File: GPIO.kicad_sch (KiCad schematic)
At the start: 8 parts, among them J12 gnd, J13 ADC, J14 Conn_01x08_Male, J15 ADC, J16 Conn_01x08_Male, J17 Conn_01x08_Male

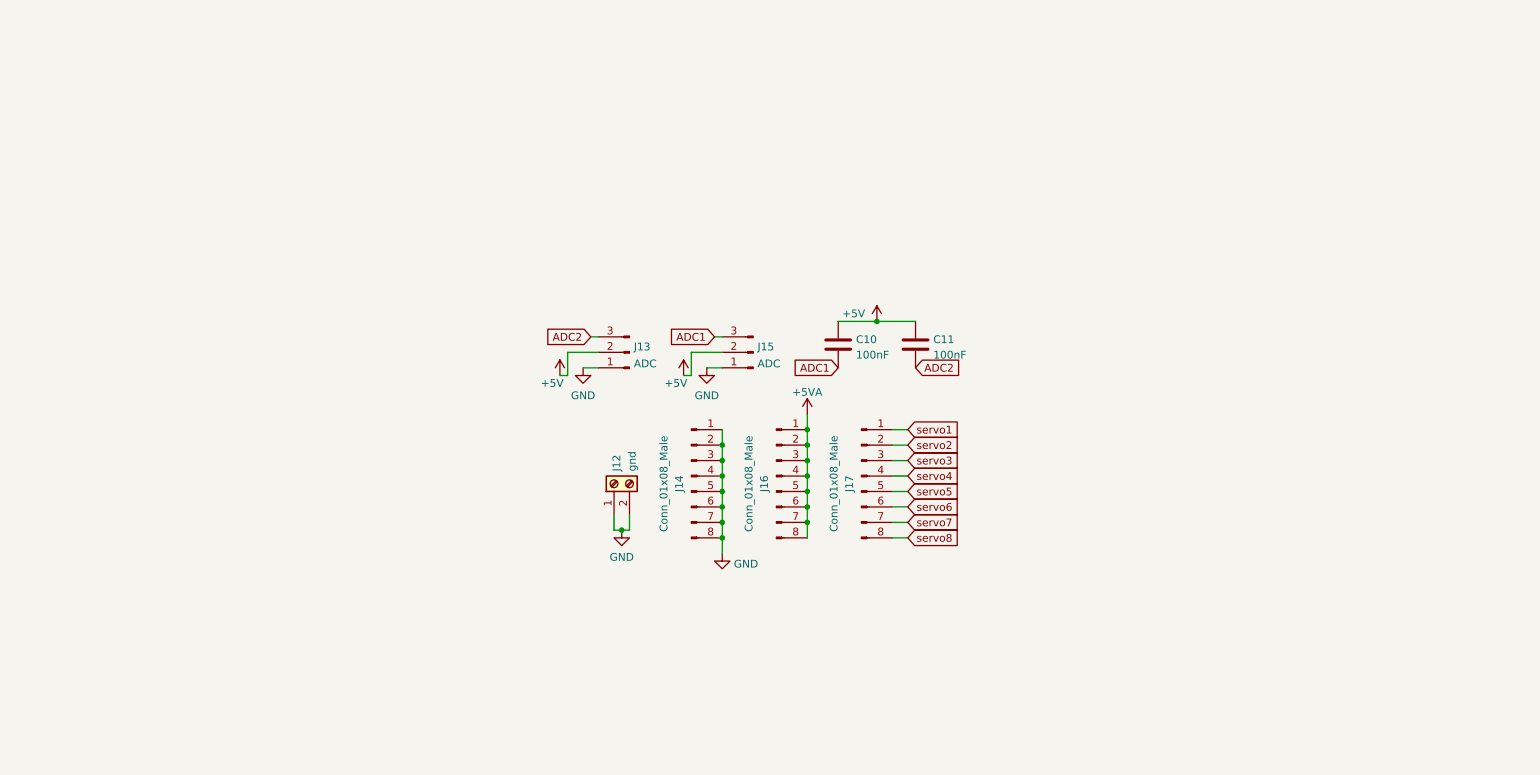
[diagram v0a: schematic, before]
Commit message: changed PCB layout. I want to change more
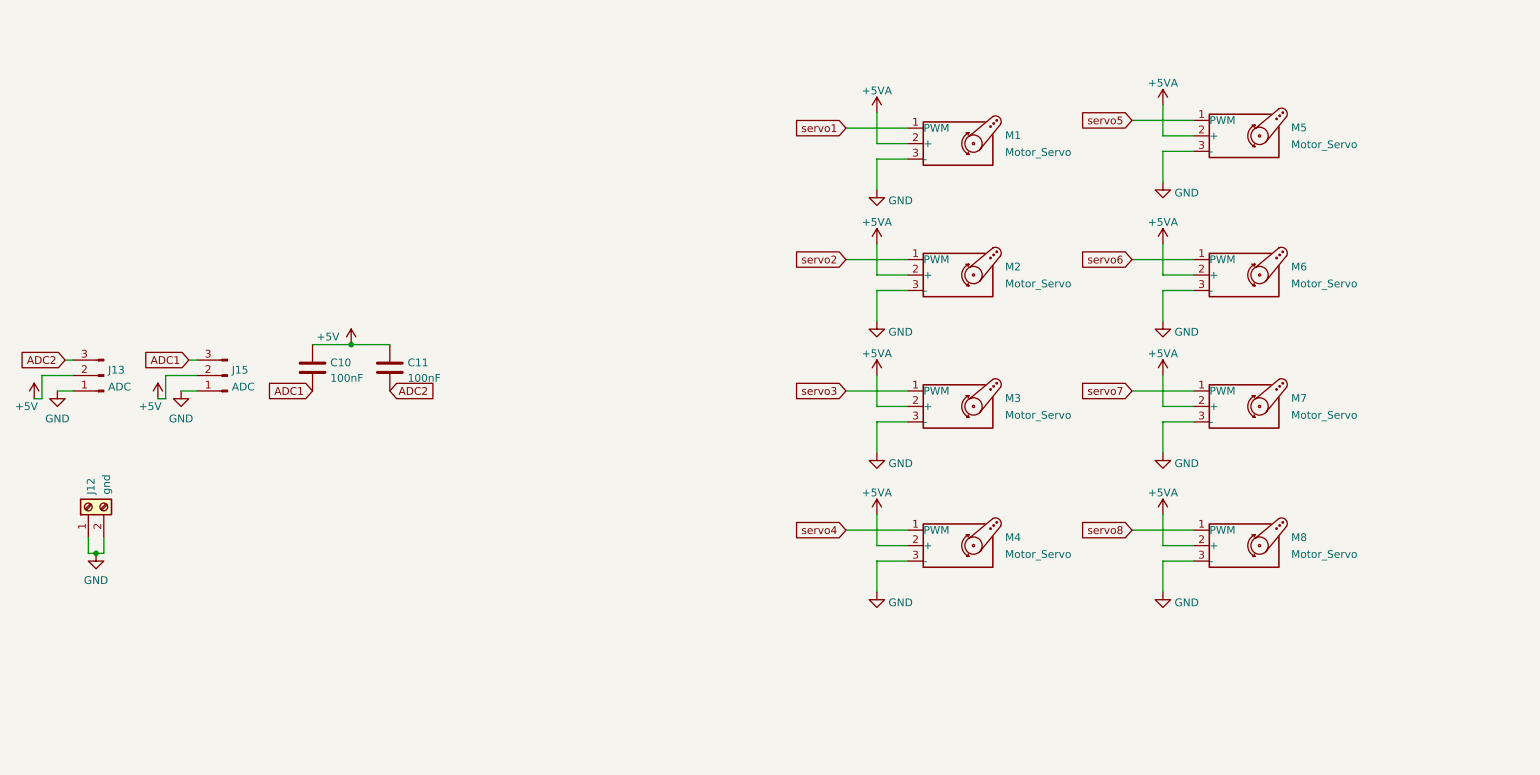
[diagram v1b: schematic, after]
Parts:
- removed J14, J16, J17: Conn_01x08_Male, Connector_PinHeader_2.54mm:PinHeader_1x08_P2.54mm_Vertical, symbol Connector:Conn_01x08_Male
- added M1, M2, M3, M4, M5, M6, M7, M8: Motor_Servo, Connector_PinHeader_2.54mm:PinHeader_1x03_P2.54mm_Vertical, symbol Motor:Motor_Servo
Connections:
- net +5VA: now also M1.2 (+), M2.2 (+), M3.2 (+), M4.2 (+), M5.2 (+), M6.2 (+), M7.2 (+), M8.2 (+)
- net GND: now also M1.3 (-), M2.3 (-), M3.3 (-), M4.3 (-), M5.3 (-), M6.3 (-), M7.3 (-), M8.3 (-)
- net servo1: now also M1.1 (PWM)
- net servo2: now also M2.1 (PWM)
- net servo3: now also M3.1 (PWM)
- net servo4: now also M4.1 (PWM)
- net servo5: now also M5.1 (PWM)
- net servo6: now also M6.1 (PWM)
- net servo7: now also M7.1 (PWM)
- net servo8: now also M8.1 (PWM)
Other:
- moved on the sheet: C10, C11, J12, J13, J15

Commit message: redone the switch connectors to accomodate a current sense print. Rearranged parts and updated silk texts to be 50% of their original size
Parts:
- removed J12: gnd, TerminalBlock_Phoenix:TerminalBlock_Phoenix_MKDS-1,5-2-5.08_1x02_P5.08mm_Horizontal, symbol Connector:Screw_Terminal_01x02
- renumbered C10 to C801, C11 to C802, J13 to J801, J15 to J802, M1 to M801, M2 to M802, M3 to M803, M4 to M804, M5 to M805, M6 to M806, M7 to M807, M8 to M808

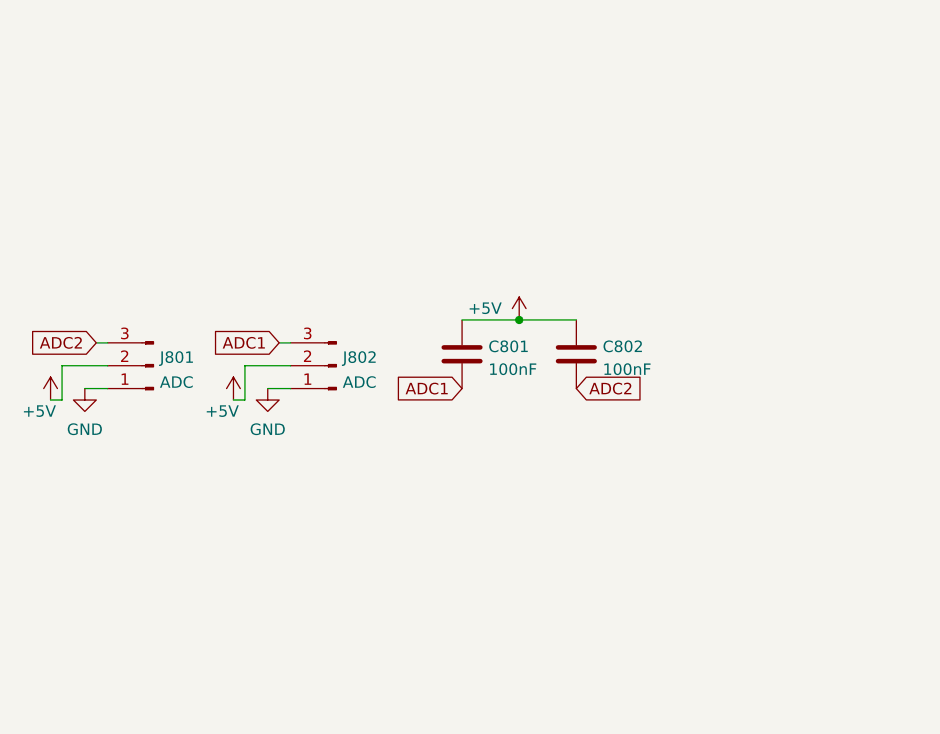
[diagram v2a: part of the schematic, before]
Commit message: added something to debug the channel buttons
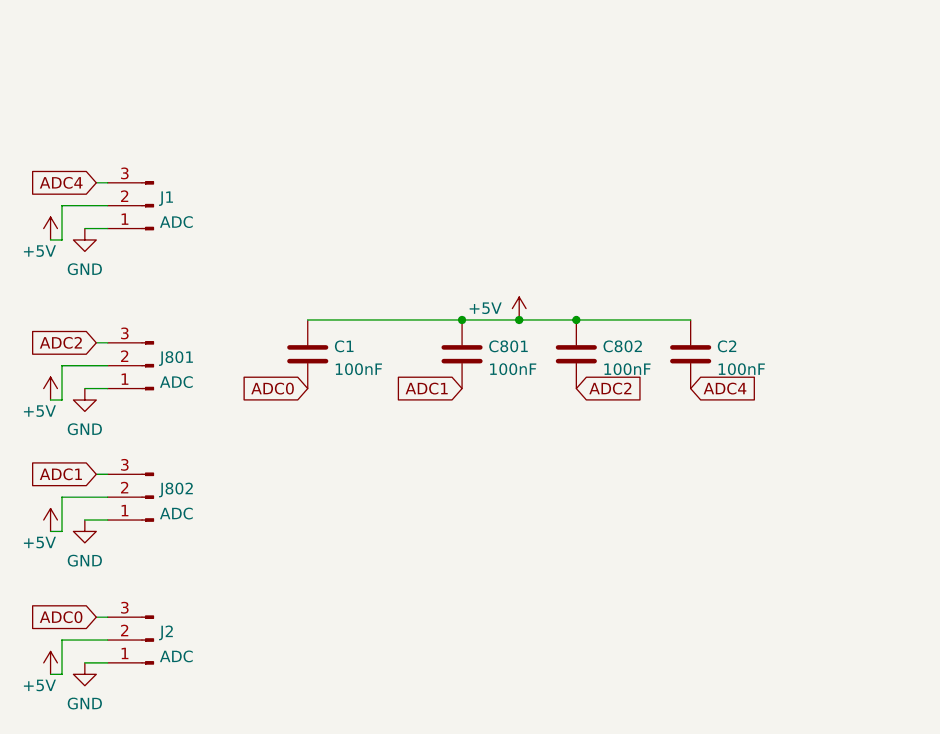
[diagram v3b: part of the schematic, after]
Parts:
- added C1, C2: 100nF, Capacitor_SMD:C_0805_2012Metric, symbol Device:C
- added J1, J2: ADC, Connector_PinHeader_2.54mm:PinHeader_1x03_P2.54mm_Vertical, symbol Connector:Conn_01x03_Male
- C801, C802: footprint Capacitor_THT:C_Disc_D3.0mm_W1.6mm_P2.50mm -> Capacitor_SMD:C_0805_2012Metric
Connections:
- net +5V: now also C1.1, C2.1, J1.2 (Pin_2), J2.2 (Pin_2)
- net GND: now also J1.1 (Pin_1), J2.1 (Pin_1)
- new net ADC0: C1.2, J2.3 (Pin_3)
- new net ADC4: C2.2, J1.3 (Pin_3)
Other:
- moved on the sheet: J802

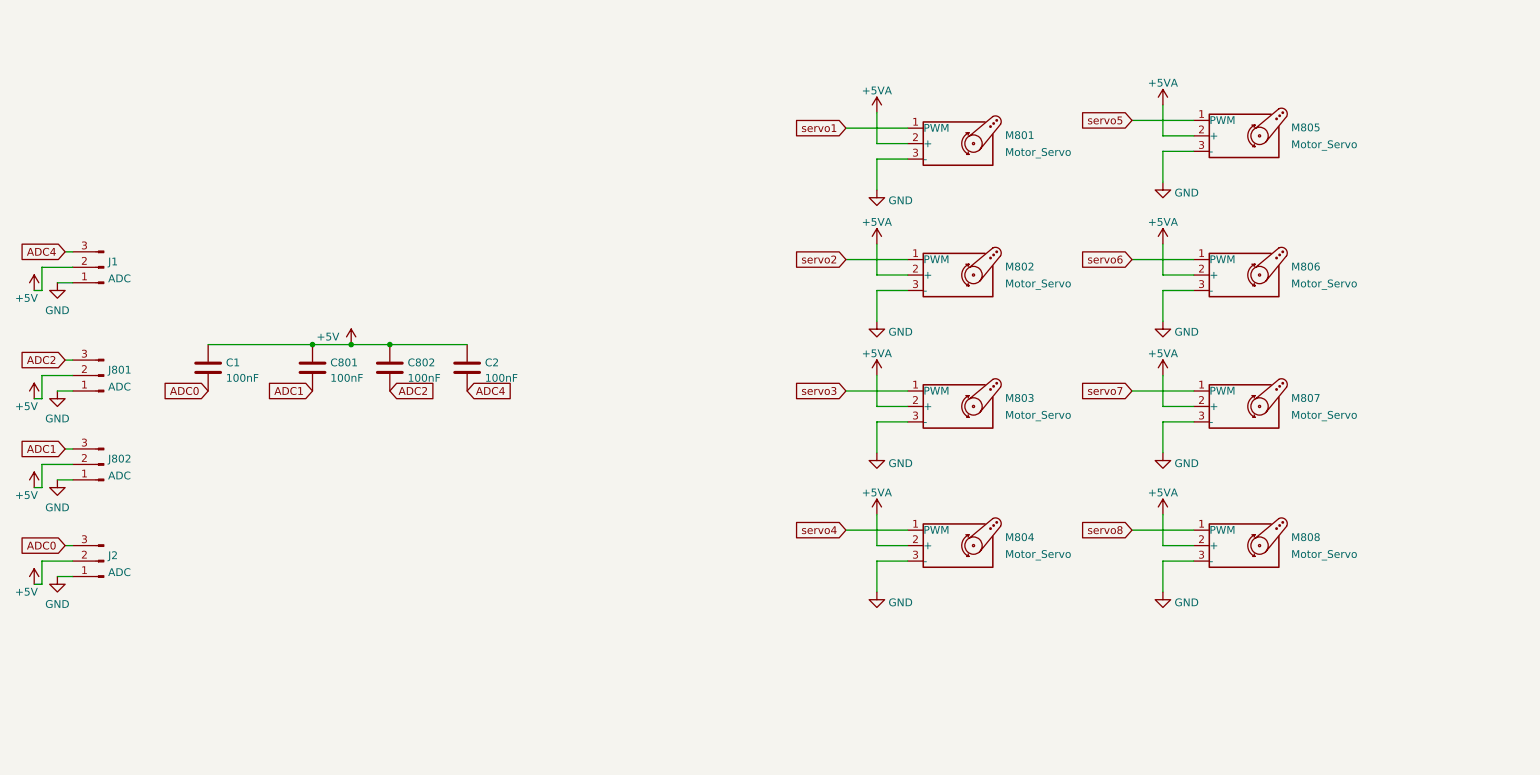
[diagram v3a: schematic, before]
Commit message: redid this project. I want to use an atmega328 so I ditched some IO. I retained 4 servo, 1 H-bridge (should make it double), 3 relays, 6 GPIO, 1 potentiometer and loconet interface. And I still have a config button
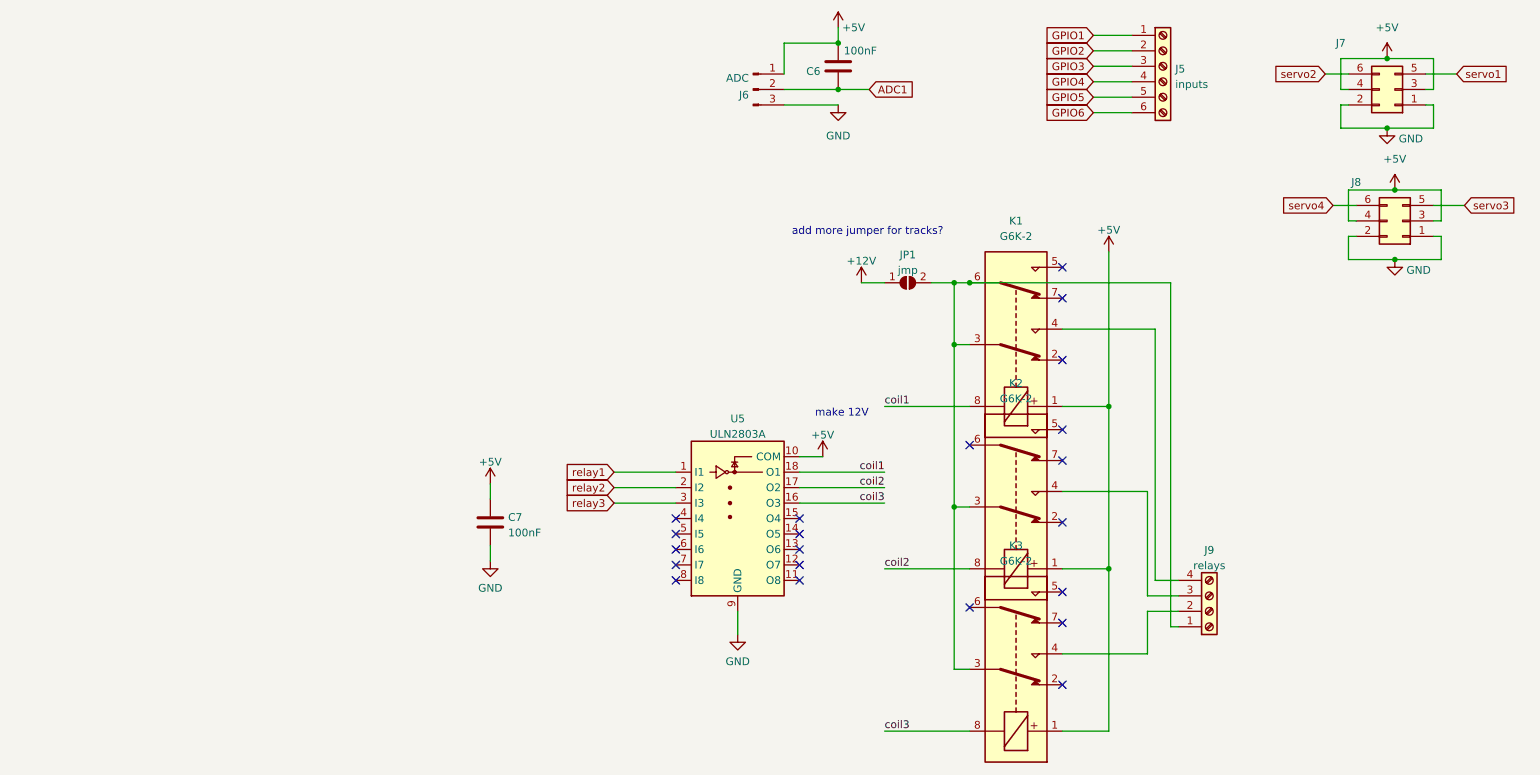
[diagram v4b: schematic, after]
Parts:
- removed C1, C2, C801, C802: 100nF, Capacitor_SMD:C_0805_2012Metric, symbol Device:C
- removed J1, J2, J801: ADC, Connector_PinHeader_2.54mm:PinHeader_1x03_P2.54mm_Vertical, symbol Connector:Conn_01x03_Male
- removed M801, M802, M803, M804, M805, M806, M807, M808: Motor_Servo, Connector_PinHeader_2.54mm:PinHeader_1x03_P2.54mm_Vertical, symbol Motor:Motor_Servo
- added C6, C7: 100nF, Capacitor_SMD:C_0805_2012Metric, symbol Device:C
- added J5: inputs, TerminalBlock_Phoenix:TerminalBlock_Phoenix_MPT-0,5-8-2.54_1x06_P2.54mm_Horizontal, symbol Connector:Screw_Terminal_01x06
- added J7, J8: Conn_02x03_Odd_Even, Connector_PinHeader_2.54mm:PinHeader_2x03_P2.54mm_Vertical_SMD, symbol Connector_Generic:Conn_02x03_Odd_Even
- added J9: relays, TerminalBlock_Phoenix:TerminalBlock_Phoenix_MKDS-1,5-4-5.08_1x04_P5.08mm_Horizontal, symbol Connector:Screw_Terminal_01x04
- added JP1: jmp, Jumper:SolderJumper-2_P1.3mm_Open_RoundedPad1.0x1.5mm, symbol Jumper:SolderJumper_2_Open
- added K1, K2, K3: G6K-2, Relay_SMD:Relay_DPDT_Omron_G6K-2F-Y, symbol Relay:G6K-2
- added U5: ULN2803A, Package_SO:SOIC-18W_7.5x11.6mm_P1.27mm, symbol Transistor_Array:ULN2803A
- renumbered J802 to J6
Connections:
- net +5V: now also J6.1 (Pin_1), C6.2, C7.1, J7.3 (Pin_3), J7.4 (Pin_4), J8.3 (Pin_3), J8.4 (Pin_4), K1.1, K2.1, K3.1, U5.10 (COM); no longer J6.2 (Pin_2)
- net ADC1: now also J6.2 (Pin_2), C6.1; no longer J6.3 (Pin_3)
- net GND: now also J6.3 (Pin_3), C7.2, J7.1 (Pin_1), J7.2 (Pin_2), J8.1 (Pin_1), J8.2 (Pin_2), U5.9 (GND); no longer J6.1 (Pin_1)
- net servo1: now also J7.5 (Pin_5)
- net servo2: now also J7.6 (Pin_6)
- net servo3: now also J8.5 (Pin_5)
- net servo4: now also J8.6 (Pin_6)
- new net: J9.1 (Pin_1), JP1.2 (B), K1.3, K1.6, K2.3, K3.3
- new net: J9.2 (Pin_2), K3.4
- new net: J9.3 (Pin_3), K2.4
- new net: J9.4 (Pin_4), K1.4
- new net +12V: JP1.1 (A)
- new net GPIO1: J5.1 (Pin_1)
- new net GPIO2: J5.2 (Pin_2)
- new net GPIO3: J5.3 (Pin_3)
- new net GPIO4: J5.4 (Pin_4)
- new net GPIO5: J5.5 (Pin_5)
- new net GPIO6: J5.6 (Pin_6)
- new net coil1: K1.8, U5.18 (O1)
- new net coil2: K2.8, U5.17 (O2)
- new net coil3: K3.8, U5.16 (O3)
- new net relay1: U5.1 (I1)
- new net relay2: U5.2 (I2)
- new net relay3: U5.3 (I3)
- no-connect marks 0 -> 21
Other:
- note added: "add more jumper for tracks?"
- note added: "make 12V"
- moved on the sheet: J6
